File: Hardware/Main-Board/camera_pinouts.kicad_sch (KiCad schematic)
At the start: 9 parts, among them J8 Conn_02x06_Odd_Even, U10 SN65LVDS050IPWRQ1, U9 SN65LVDS1DBV

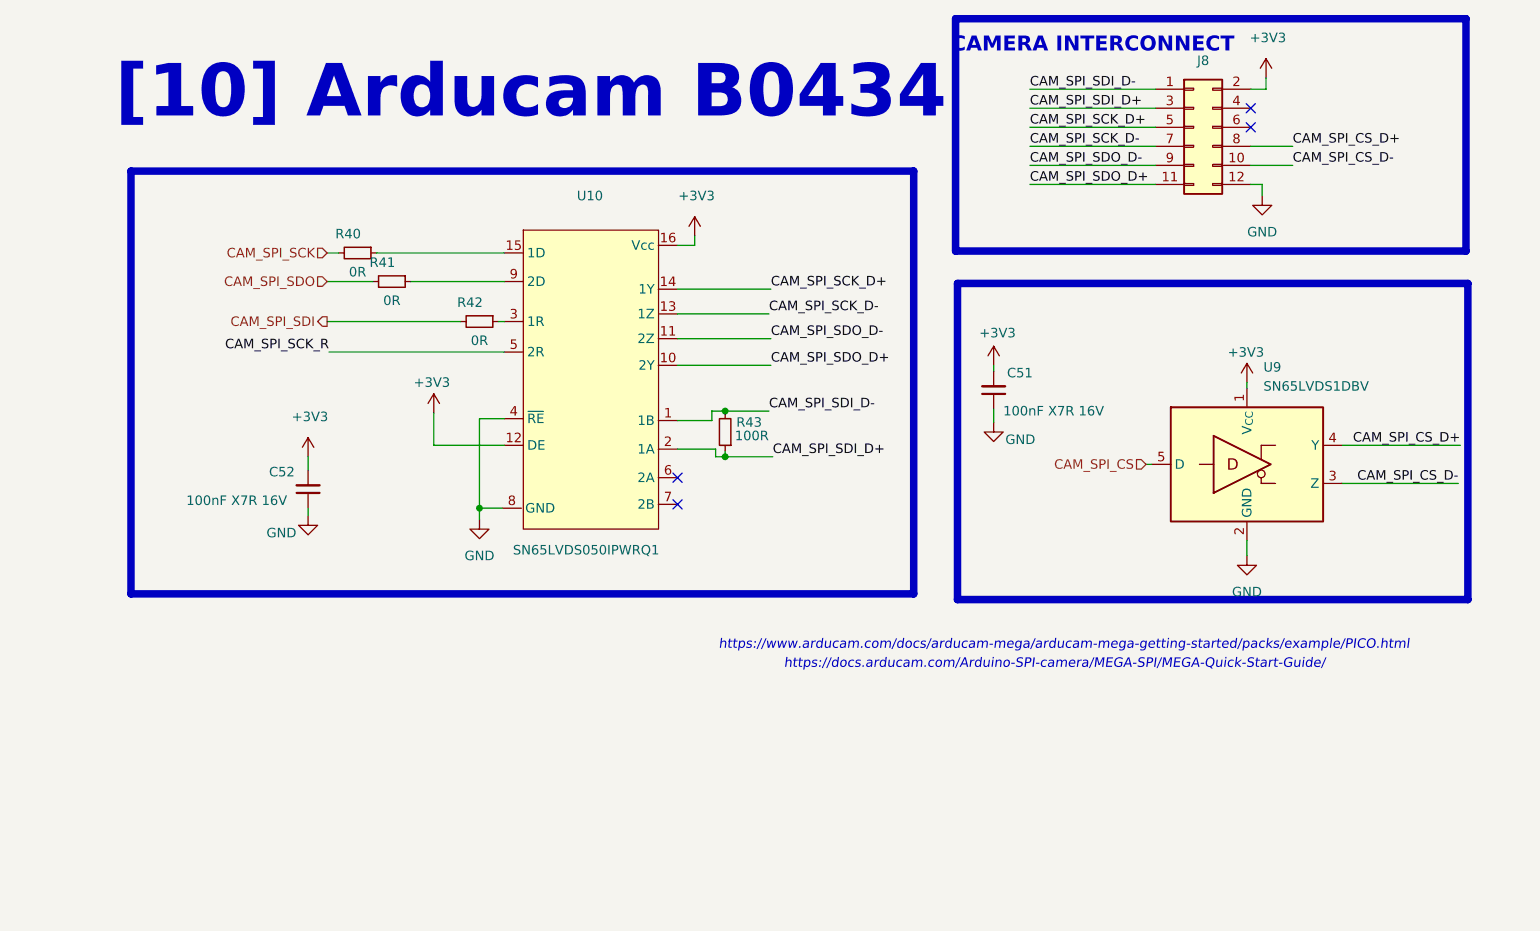
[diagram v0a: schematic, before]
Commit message: Done with main board design, and camera interconnect in progress
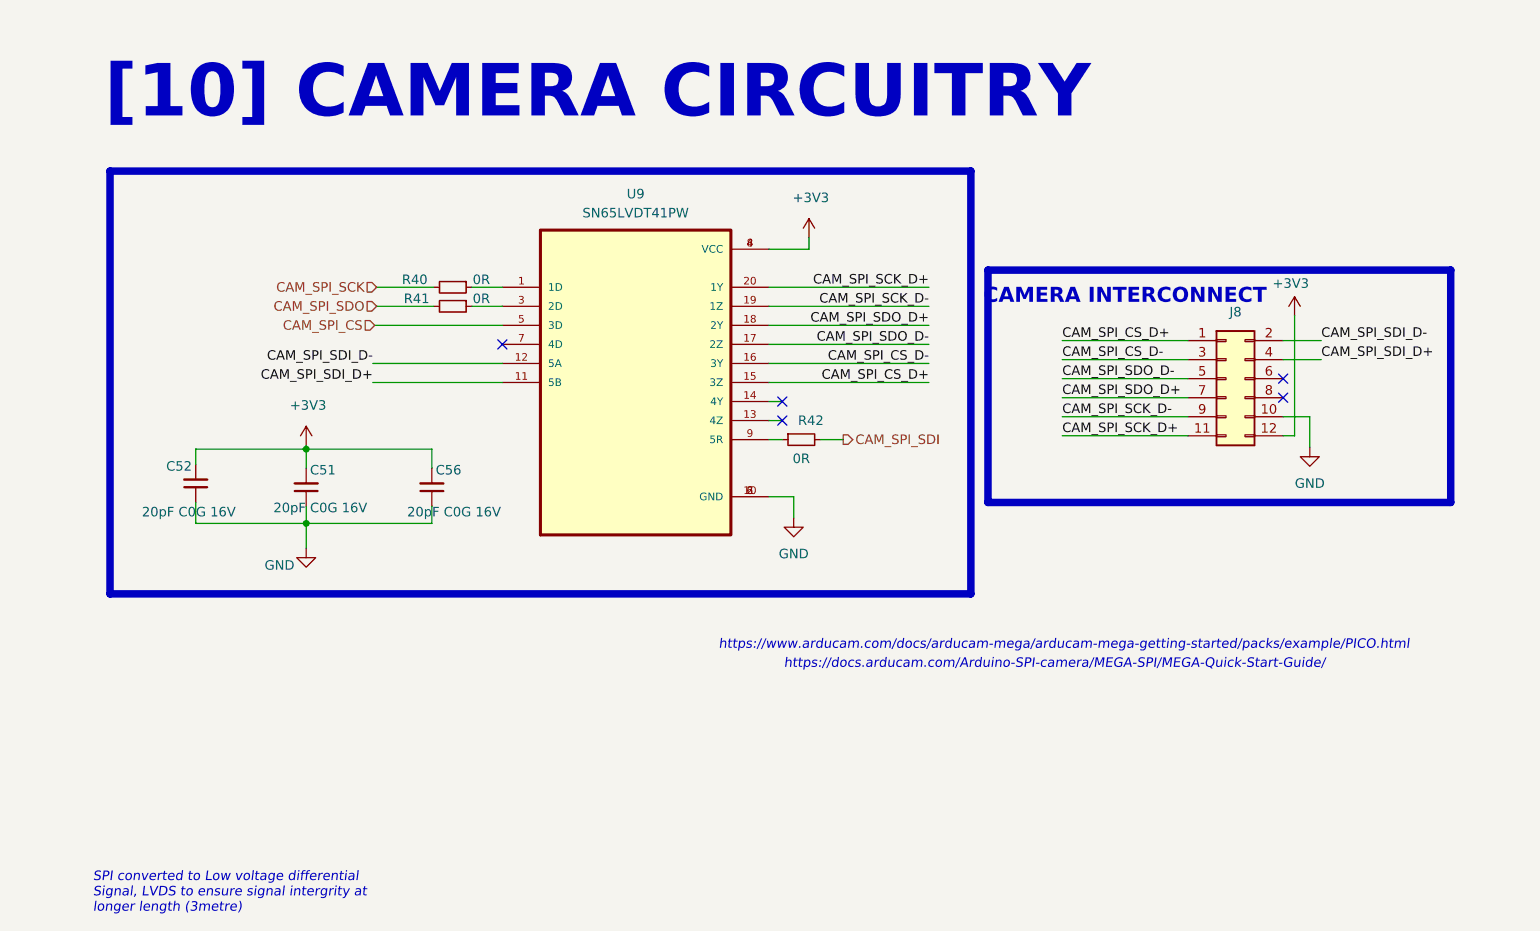
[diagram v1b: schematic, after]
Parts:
- removed R43: 100R, Resistor_SMD:R_0402_1005Metric, symbol Device:R_Small
- removed U10: SN65LVDS050IPWRQ1, Package_SO:TSSOP-16_4.4x5mm_P0.65mm, symbol powerLabs_Lib_hassan:SN65LVDS050IPWRQ1
- removed U9: SN65LVDS1DBV, Package_TO_SOT_SMD:SOT-23-5, symbol Interface:SN65LVDS1DBV
- added C56: 20pF C0G 16V, Capacitor_SMD:C_0402_1005Metric, symbol Device:C_Small
- added U9: SN65LVDT41PW, SN65LVDT41PW:SOP65P640X120-20N, symbol SN65LVDT41PW:SN65LVDT41PW
- C51, C52: value 100nF X7R 16V -> 20pF C0G 16V
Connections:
- net +3V3: now also J8.12 (Pin_12), C56.2, U9.4 (VCC), U9.8 (VCC); no longer J8.2 (Pin_2)
- net CAM_SPI_CS: now also U9.5 (3D)
- net CAM_SPI_CS_D+: now also J8.1 (Pin_1), U9.15 (3Z); no longer J8.8 (Pin_8)
- net CAM_SPI_CS_D-: now also J8.3 (Pin_3), U9.16 (3Y); no longer J8.10 (Pin_10)
- net CAM_SPI_SCK_D+: now also J8.11 (Pin_11), U9.20 (1Y); no longer J8.5 (Pin_5)
- net CAM_SPI_SCK_D-: now also J8.9 (Pin_9), U9.19 (1Z); no longer J8.7 (Pin_7)
- net CAM_SPI_SDI_D+: now also J8.4 (Pin_4), U9.11 (5B); no longer J8.3 (Pin_3)
- net CAM_SPI_SDI_D-: now also J8.2 (Pin_2), U9.12 (5A); no longer J8.1 (Pin_1)
- net CAM_SPI_SDO_D+: now also J8.7 (Pin_7), U9.18 (2Y); no longer J8.11 (Pin_11)
- net CAM_SPI_SDO_D-: now also J8.5 (Pin_5), U9.17 (2Z); no longer J8.9 (Pin_9)
- net GND: now also J8.10 (Pin_10), C56.1, U9.10 (GND), U9.2 (GND), U9.6 (GND); no longer J8.12 (Pin_12)
- net at R40.1: now also U9.1 (1D)
- net at R42.1: now also U9.9 (5R)
- net at R41.1: now also U9.3 (2D)
- no-connect marks 4 -> 5
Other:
- note added: "SPI converted to Low voltage differential Signal, LVDS to ensure signal intergrity at longer length (3metre)"
- note added: "[10] CAMERA CIRCUITRY"
- note removed: "[10] Arducam B0434"
- moved on the sheet: J8

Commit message: Updated the pdf for main board schematics
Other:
- note added: "Add the simulation for capacitor impedande characteristics graph"
- note added: "Differential lines are internally terminated with 100R resistors"
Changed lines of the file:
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@@
 	)
 	(image
-		(at 74.422 118.364)
-		(scale 0.807911)
+		(at 73.914 125.73)
+		(scale 0.525238)
 		(data "iVBORw0KGgoAAAANSUhEUgAAAZsAAAGcCAYAAAAPnQ1AAAAABHNCSVQICAgIfAhkiAAAABl0RVh0"
 			"U29mdHdhcmUAZ25vbWUtc2NyZWVuc2hvdO8Dvz4AAAAmdEVYdENyZWF0aW9uIFRpbWUAVGh1IDA2"
@@
 		)
 	)
+	(text "Add the simulation for capacitor\nimpedande characteristics graph"
+		(exclude_from_sim no)
+		(at 44.45 87.63 0)
+		(effects
+			(font
+				(size 1.27 1.27)
+				(italic yes)
+				(color 138 138 138 1)
+			)
+			(justify left)
+		)
+	)
+	(text "Differential lines are internally \nterminated with 100R resistors"
+		(exclude_from_sim no)
+		(at 12.7 121.92 0)
+		(effects
+			(font
+				(size 1.27 1.27)
+				(italic yes)
+				(color 138 138 138 1)
+			)
+			(justify left)
+		)
+	)
